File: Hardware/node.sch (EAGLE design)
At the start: 47 parts, among them J1 USB_B, M1 SERVO, M2 SERVO, Q1 16MHz, U1 MAX3485CSA

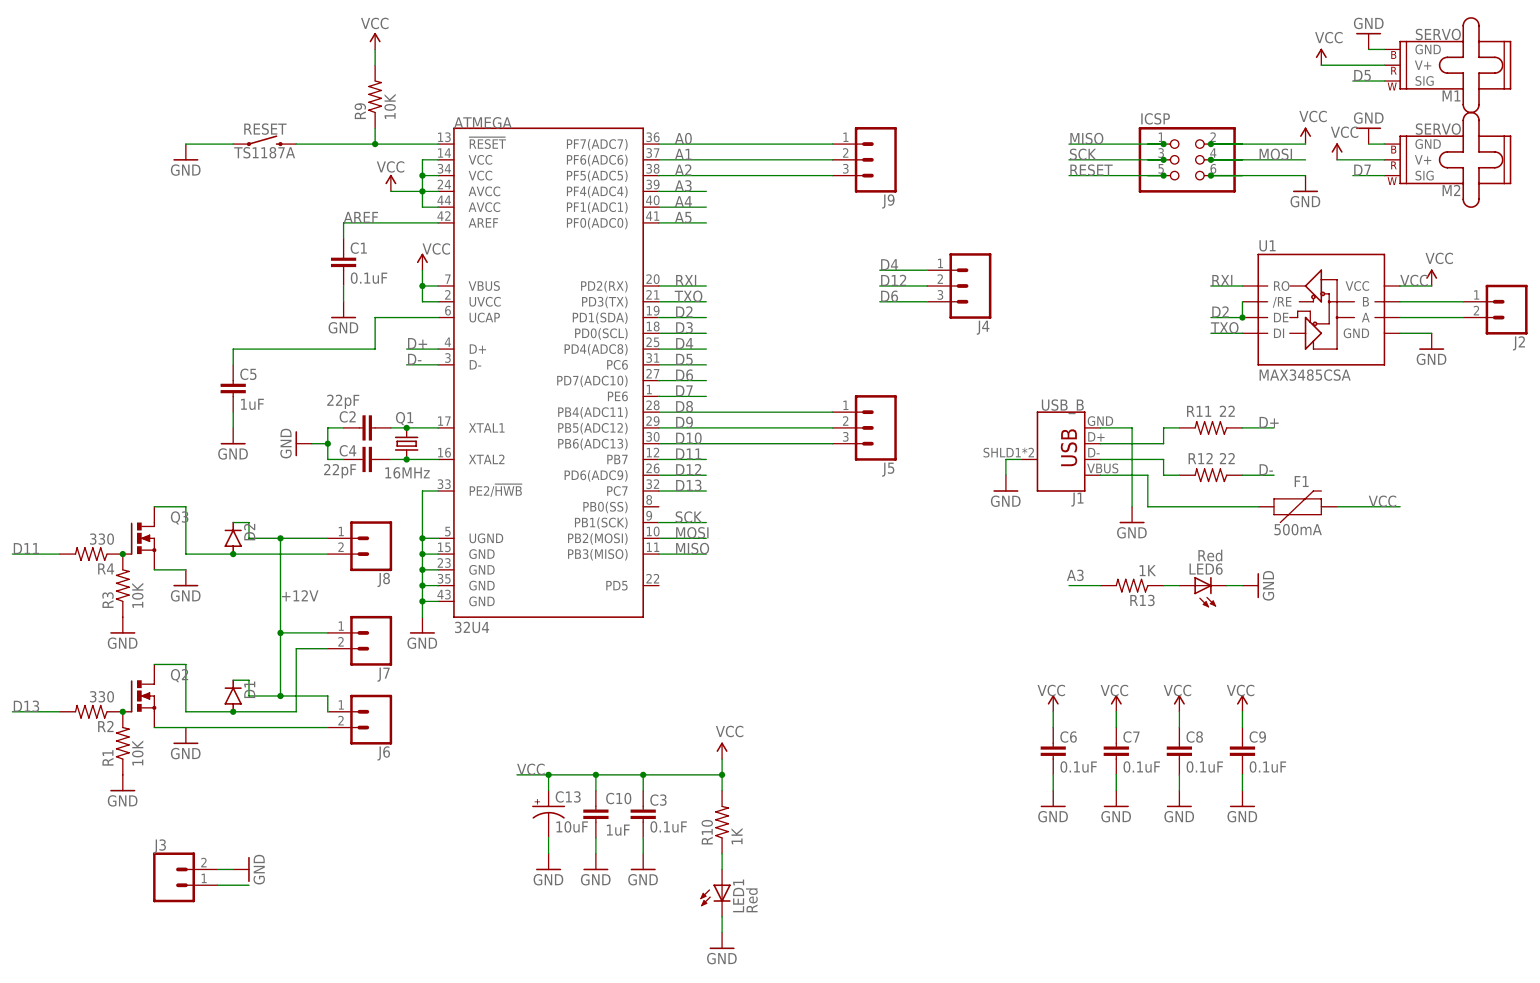
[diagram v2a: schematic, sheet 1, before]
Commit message: Finalize hardware design and add production files
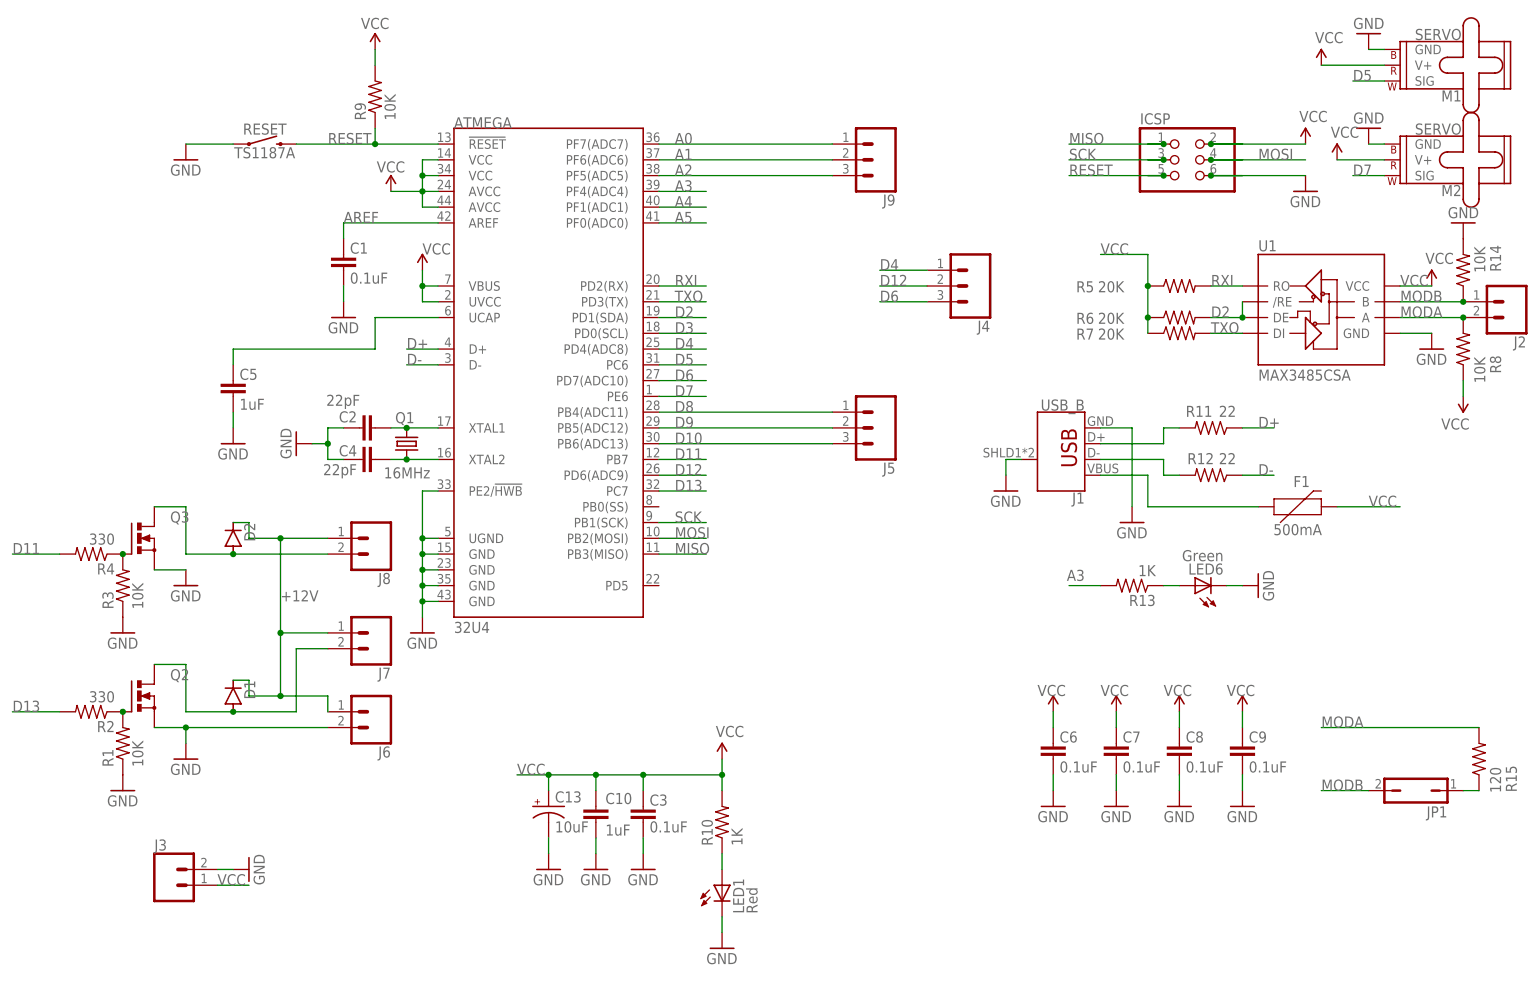
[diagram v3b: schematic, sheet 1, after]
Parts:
- added JP1: (no value), jumper:JP1Q
- added R14, R8: 10K, SparkFun:RESISTOR0603-RES
- added R15: 120, SparkFun:RESISTOR0603-RES
- added R5, R6, R7: 20K, SparkFun:RESISTOR0603-RES
- LED6: value Red -> Green
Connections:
- removed net N$5: J2.2, U1.A
- new net MODA: J2.2, R15.2, R8.2, U1.A
- new net MODB: J2.1, JP1.2, R14.1, U1.B
- net D2: now also R6.2
- net GND: now also R14.2
- net N$3: now also JP1.1, R15.1; no longer J2.1, U1.B
- net RXI: now also R5.2
- net TXO: now also R7.2
- net VCC: now also R5.1, R6.1, R7.1, R8.1
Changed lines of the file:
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@@
 <part name="GND22" library="SparkFun" deviceset="GND" device=""/>
 <part name="R13" library="SparkFun" deviceset="RESISTOR" device="0603-RES" value="1K"/>
-<part name="LED6" library="SparkFun" deviceset="LED" device="0603" value="Red"/>
+<part name="LED6" library="SparkFun" deviceset="LED" device="0603" value="Green"/>
 <part name="GND23" library="SparkFun" deviceset="GND" device=""/>
 <part name="Q1" library="crystal-geyer_V1_0" library_urn="urn:adsk.eagle:library:203" deviceset="KX" device="-7" package3d_urn="urn:adsk.eagle:package:11924/1" value="16MHz"/>
-<part name="GND24" library="SparkFun" deviceset="GND" device=""/>
 <part name="F1" library="SparkFun-Fuses" library_urn="urn:adsk.eagle:library:517" deviceset="PPTC" device="_HALF-AMP" package3d_urn="urn:adsk.eagle:package:38575/1" value="500mA"/>
 <part name="RESET" library="SparkFun-Switches" library_urn="urn:adsk.eagle:library:535" deviceset="MOMENTARY-SWITCH-SPST" device="-SMD-5.2MM" package3d_urn="urn:adsk.eagle:package:40167/1" value="TS1187A"/>
@@
 <part name="J8" library="SparkFun-Connectors" library_urn="urn:adsk.eagle:library:513" deviceset="CONN_02" device="5MM" package3d_urn="urn:adsk.eagle:package:38044/1"/>
 <part name="J9" library="SparkFun-Connectors" library_urn="urn:adsk.eagle:library:513" deviceset="CONN_03" device="-SCREW-5MM" package3d_urn="urn:adsk.eagle:package:38070/1"/>
+<part name="R5" library="SparkFun" deviceset="RESISTOR" device="0603-RES" value="20K"/>
+<part name="R6" library="SparkFun" deviceset="RESISTOR" device="0603-RES" value="20K"/>
+<part name="R7" library="SparkFun" deviceset="RESISTOR" device="0603-RES" value="20K"/>
+<part name="R8" library="SparkFun" deviceset="RESISTOR" device="0603-RES" value="10K"/>
+<part name="R14" library="SparkFun" deviceset="RESISTOR" device="0603-RES" value="10K"/>
+<part name="GND18" library="SparkFun" deviceset="GND" device=""/>
+<part name="P+6" library="SparkFun" deviceset="3.3V" device="" value="VCC"/>
+<part name="JP1" library="jumper" library_urn="urn:adsk.eagle:library:252" deviceset="JP1Q" device="" package3d_urn="urn:adsk.eagle:package:15455/1"/>
+<part name="R15" library="SparkFun" deviceset="RESISTOR" device="0603-RES" value="120"/>
 </parts>
 <sheets>
@@
 <attribute name="VALUE" x="42.037" y="66.04" size="1.778" layer="96" rot="R270"/>
 </instance>
-<instance part="GND15" gate="1" x="38.1" y="55.88" smashed="yes">
-<attribute name="VALUE" x="35.56" y="53.34" size="1.778" layer="96"/>
+<instance part="GND15" gate="1" x="38.1" y="53.34" smashed="yes">
+<attribute name="VALUE" x="35.56" y="50.8" size="1.778" layer="96"/>
 </instance>
 <instance part="J6" gate="G$1" x="68.58" y="60.96" smashed="yes" rot="R180">
@@
 <attribute name="VALUE" x="152.4" y="157.226" size="1.778" layer="96" font="vector" rot="R180"/>
 <attribute name="NAME" x="152.4" y="144.272" size="1.778" layer="95" font="vector" rot="R180"/>
+</instance>
+<instance part="R5" gate="G$1" x="198.12" y="129.54" smashed="yes">
+<attribute name="NAME" x="184.404" y="130.302" size="1.778" layer="95" rot="R180"/>
+<attribute name="VALUE" x="189.23" y="130.302" size="1.778" layer="96" rot="R180"/>
+</instance>
+<instance part="R6" gate="G$1" x="198.12" y="124.46" smashed="yes">
+<attribute name="NAME" x="184.404" y="125.222" size="1.778" layer="95" rot="R180"/>
+<attribute name="VALUE" x="189.23" y="125.222" size="1.778" layer="96" rot="R180"/>
+</instance>
+<instance part="R7" gate="G$1" x="198.12" y="121.92" smashed="yes">
+<attribute name="NAME" x="184.404" y="122.682" size="1.778" layer="95" rot="R180"/>
+<attribute name="VALUE" x="189.23" y="122.682" size="1.778" layer="96" rot="R180"/>
+</instance>
+<instance part="R8" gate="G$1" x="243.84" y="119.38" smashed="yes" rot="R90">
+<attribute name="NAME" x="248.158" y="118.364" size="1.778" layer="95" rot="R270"/>
+<attribute name="VALUE" x="245.618" y="118.11" size="1.778" layer="96" rot="R270"/>
+</instance>
+<instance part="R14" gate="G$1" x="243.84" y="132.08" smashed="yes" rot="R90">
+<attribute name="NAME" x="248.158" y="136.144" size="1.778" layer="95" rot="R270"/>
+<attribute name="VALUE" x="245.618" y="135.89" size="1.778" layer="96" rot="R270"/>
+</instance>
+<instance part="GND18" gate="1" x="243.84" y="139.7" smashed="yes" rot="R180">
+<attribute name="VALUE" x="246.38" y="142.24" size="1.778" layer="96" rot="R180"/>
+</instance>
+<instance part="P+6" gate="G$1" x="243.84" y="111.76" smashed="yes" rot="R180">
+<attribute name="VALUE" x="244.856" y="108.204" size="1.778" layer="96" rot="R180"/>
+</instance>
+<instance part="JP1" gate="A" x="236.22" y="48.26" smashed="yes" rot="R90">
+<attribute name="NAME" x="241.3" y="45.72" size="1.778" layer="95" rot="R180"/>
+<attribute name="VALUE" x="241.3" y="52.705" size="1.778" layer="96" rot="R180"/>
+</instance>
+<instance part="R15" gate="G$1" x="246.38" y="53.34" smashed="yes" rot="R90">
+<attribute name="NAME" x="250.698" y="52.324" size="1.778" layer="95" rot="R270"/>
+<attribute name="VALUE" x="248.158" y="52.07" size="1.778" layer="96" rot="R270"/>
 </instance>
 </instances>
@@
 <pinref part="Q2" gate="G$1" pin="S"/>
 <pinref part="GND15" gate="1" pin="GND"/>
-<wire x1="38.1" y1="58.42" x2="33.02" y2="58.42" width="0.1524" layer="91"/>
-<wire x1="60.96" y1="58.42" x2="38.1" y2="58.42" width="0.1524" layer="91"/>
 <pinref part="J6" gate="G$1" pin="2"/>
+<wire x1="33.02" y1="58.42" x2="38.1" y2="58.42" width="0.1524" layer="91"/>
+<wire x1="38.1" y1="58.42" x2="38.1" y2="55.88" width="0.1524" layer="91"/>
+<wire x1="38.1" y1="58.42" x2="60.96" y2="58.42" width="0.1524" layer="91"/>
+<junction x="38.1" y="58.42"/>
 </segment>
 <segment>
@@
 <pinref part="GND12" gate="1" pin="GND"/>
 <wire x1="45.72" y1="35.56" x2="43.18" y2="35.56" width="0.1524" layer="91"/>
+</segment>
+<segment>
+<pinref part="R14" gate="G$1" pin="2"/>
+<pinref part="GND18" gate="1" pin="GND"/>
 </segment>
 </net>
@@
 <pinref part="ATMEGA" gate="G$1" pin="!RESET"/>
 <pinref part="RESET" gate="G$1" pin="2"/>
+<label x="60.96" y="152.4" size="1.778" layer="95"/>
 </segment>
 <segment>
@@
 <pinref part="U1" gate="G$1" pin="DI"/>
 <wire x1="203.2" y1="121.92" x2="208.28" y2="121.92" width="0.1524" layer="91"/>
+<pinref part="R7" gate="G$1" pin="2"/>
 </segment>
 </net>
@@
 <pinref part="J3" gate="G$1" pin="1"/>
 <wire x1="43.18" y1="33.02" x2="48.26" y2="33.02" width="0.1524" layer="91"/>
+<label x="43.18" y="33.02" size="1.778" layer="95"/>
+</segment>
+<segment>
+<pinref part="R7" gate="G$1" pin="1"/>
+<pinref part="R6" gate="G$1" pin="1"/>
+<wire x1="193.04" y1="121.92" x2="193.04" y2="124.46" width="0.1524" layer="91"/>
+<pinref part="R5" gate="G$1" pin="1"/>
+<wire x1="193.04" y1="129.54" x2="193.04" y2="124.46" width="0.1524" layer="91"/>
+<junction x="193.04" y="124.46"/>
+<wire x1="193.04" y1="129.54" x2="193.04" y2="134.62" width="0.1524" layer="91"/>
+<wire x1="193.04" y1="134.62" x2="185.42" y2="134.62" width="0.1524" layer="91"/>
+<junction x="193.04" y="129.54"/>
+<label x="185.42" y="134.62" size="1.778" layer="95"/>
+</segment>
+<segment>
+<pinref part="R8" gate="G$1" pin="1"/>
+<pinref part="P+6" gate="G$1" pin="3.3V"/>
+<wire x1="243.84" y1="111.76" x2="243.84" y2="114.3" width="0.1524" layer="91"/>
 </segment>
 </net>
@@
 <junction x="208.28" y="124.46"/>
 <label x="203.2" y="124.46" size="1.778" layer="95"/>
+<pinref part="R6" gate="G$1" pin="2"/>
 </segment>
 </net>
@@
 <pinref part="U1" gate="G$1" pin="RO"/>
 <wire x1="203.2" y1="129.54" x2="208.28" y2="129.54" width="0.1524" layer="91"/>
+<pinref part="R5" gate="G$1" pin="2"/>
 </segment>
 </net>
@@
 </segment>
 </net>
-<net name="N$3" class="0">
+<net name="MODB" class="0">
 <segment>
 <pinref part="U1" gate="G$1" pin="B"/>
 <pinref part="J2" gate="G$1" pin="1"/>
 <wire x1="233.68" y1="127" x2="243.84" y2="127" width="0.1524" layer="91"/>
-</segment>
-</net>
-<net name="N$5" class="0">
+<pinref part="R14" gate="G$1" pin="1"/>
+<junction x="243.84" y="127"/>
+<label x="233.68" y="127" size="1.778" layer="95"/>
+</segment>
+<segment>
+<pinref part="JP1" gate="A" pin="2"/>
+<wire x1="228.6" y1="48.26" x2="220.98" y2="48.26" width="0.1524" layer="91"/>
+<label x="220.98" y="48.26" size="1.778" layer="95"/>
+</segment>
+</net>
+<net name="MODA" class="0">
 <segment>
 <pinref part="J2" gate="G$1" pin="2"/>
 <pinref part="U1" gate="G$1" pin="A"/>
 <wire x1="243.84" y1="124.46" x2="233.68" y2="124.46" width="0.1524" layer="91"/>
+<pinref part="R8" gate="G$1" pin="2"/>
+<junction x="243.84" y="124.46"/>
+<label x="233.68" y="124.46" size="1.778" layer="95"/>
+</segment>
+<segment>
+<pinref part="R15" gate="G$1" pin="2"/>
+<wire x1="246.38" y1="58.42" x2="220.98" y2="58.42" width="0.1524" layer="91"/>
+<label x="220.98" y="58.42" size="1.778" layer="95"/>
 </segment>
 </net>
@@
 </segment>
 </net>
+<net name="N$3" class="0">
+<segment>
+<pinref part="JP1" gate="A" pin="1"/>
+<pinref part="R15" gate="G$1" pin="1"/>
+<wire x1="246.38" y1="48.26" x2="243.84" y2="48.26" width="0.1524" layer="91"/>
+</segment>
+</net>
 </nets>
 </sheet>
@@
 <attribute name="VALUE" x="129.032" y="12.7762" size="1.778" layer="96"/>
 </instance>
-<instance part="GND24" gate="1" x="40.64" y="38.1" smashed="yes">
-<attribute name="VALUE" x="38.1" y="35.56" size="1.778" layer="96"/>
-</instance>
 </instances>
 <busses>
 </busses>
 <nets>
-<net name="GND" class="1">
-<segment>
-<wire x1="33.02" y1="40.64" x2="40.64" y2="40.64" width="0.1524" layer="91"/>
-<pinref part="GND24" gate="1" pin="GND"/>
-</segment>
-</net>
-<net name="RAW" class="1">
-<segment>
-<wire x1="33.02" y1="43.18" x2="40.64" y2="43.18" width="0.1524" layer="91"/>
-<label x="38.1" y="43.18" size="1.778" layer="95"/>
-</segment>
-</net>
 </nets>
 </sheet>
